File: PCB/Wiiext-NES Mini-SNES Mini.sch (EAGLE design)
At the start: 16 parts, among them J1 USB4085-GF-A_REVA4

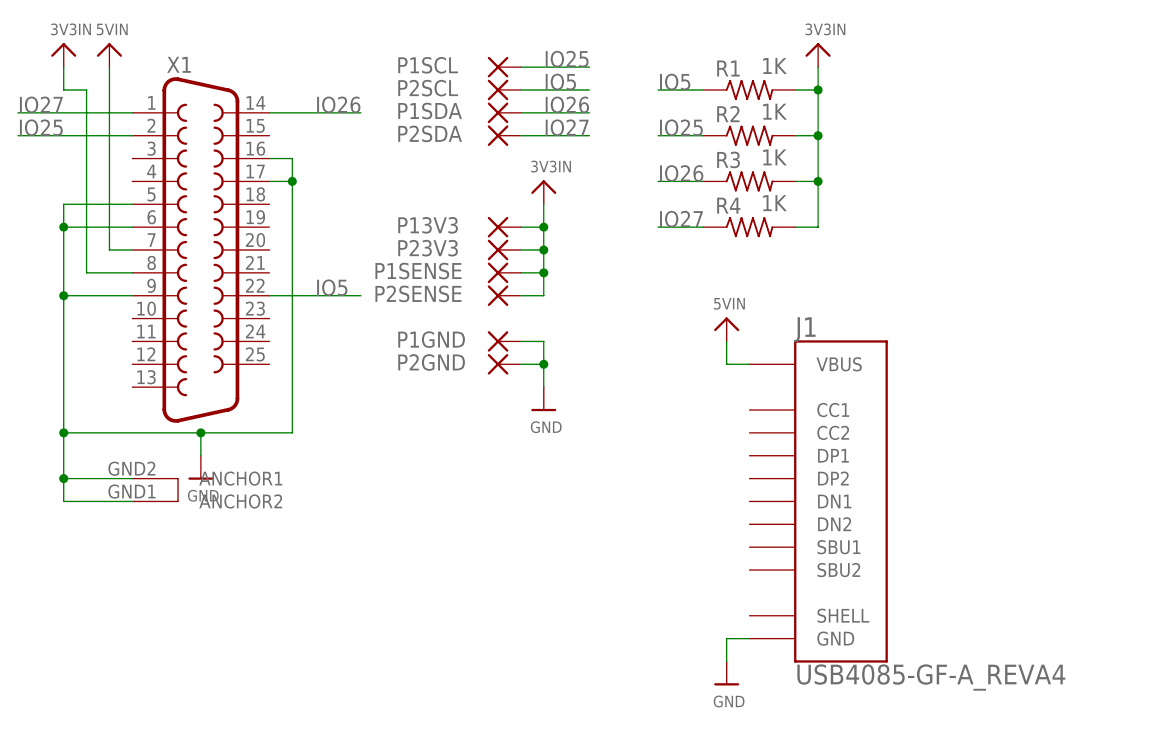
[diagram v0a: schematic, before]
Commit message: Add Support for 5V PD Chargers (#61)
Added 5.1K pull down resistors on the CC1 and CC2 to enable the use of a PD charger for 5V charging.  Also cleaned up the PCB design and spread out pads for easier assembly.
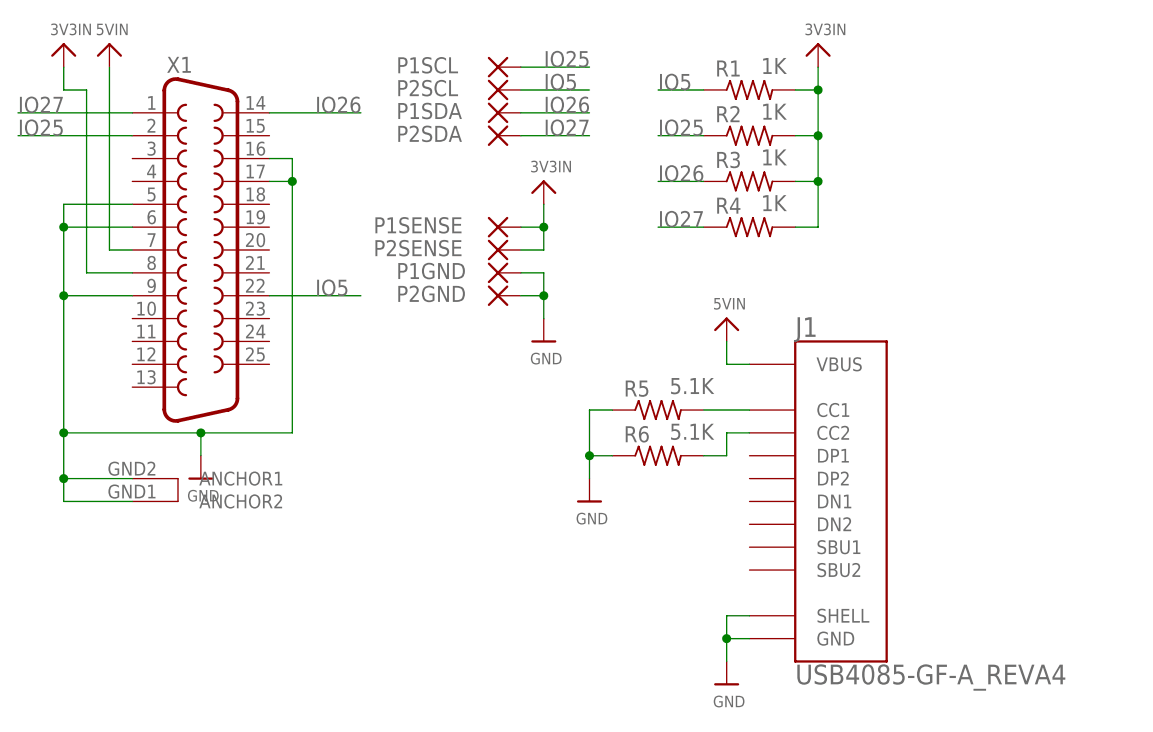
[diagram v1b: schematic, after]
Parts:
- removed P13V3, P23V3: (no value), wirepad:SMD5
- added R5, R6: 5.1K, adafruit:R-US_R1206
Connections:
- new net PD1: J1.CC2, R6.2
- new net PD2: J1.CC1, R5.2
- net 3V3IN: no longer P13V3.P, P23V3.P
- net GND: now also J1.SHELL, R5.1, R6.1
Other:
- moved on the sheet: P1GND, P1SENSE, P2GND, P2SENSE
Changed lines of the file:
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@@
 <part name="P1SDA" library="wirepad" library_urn="urn:adsk.eagle:library:412" deviceset="SMD5" device="" package3d_urn="urn:adsk.eagle:package:30841/1"/>
 <part name="P2SDA" library="wirepad" library_urn="urn:adsk.eagle:library:412" deviceset="SMD5" device="" package3d_urn="urn:adsk.eagle:package:30841/1"/>
-<part name="P13V3" library="wirepad" library_urn="urn:adsk.eagle:library:412" deviceset="SMD5" device="" package3d_urn="urn:adsk.eagle:package:30841/1"/>
-<part name="P23V3" library="wirepad" library_urn="urn:adsk.eagle:library:412" deviceset="SMD5" device="" package3d_urn="urn:adsk.eagle:package:30841/1"/>
 <part name="P1SENSE" library="wirepad" library_urn="urn:adsk.eagle:library:412" deviceset="SMD5" device="" package3d_urn="urn:adsk.eagle:package:30841/1"/>
 <part name="P1GND" library="wirepad" library_urn="urn:adsk.eagle:library:412" deviceset="SMD5" device="" package3d_urn="urn:adsk.eagle:package:30841/1"/>
@@
 <part name="U$4" library="Airquality_Sensor" library_urn="urn:adsk.eagle:library:16015176" deviceset="GND" device=""/>
 <part name="U$5" library="microbuilder" deviceset="VIN" device="" value="3V3IN"/>
+<part name="R5" library="adafruit" deviceset="R-US_" device="R1206" value="5.1K"/>
+<part name="R6" library="adafruit" deviceset="R-US_" device="R1206" value="5.1K"/>
+<part name="U$6" library="Airquality_Sensor" library_urn="urn:adsk.eagle:library:16015176" deviceset="GND" device=""/>
 </parts>
 <sheets>
@@
 <attribute name="VALUE" x="445.897" y="-3.302" size="1.778" layer="96"/>
 </instance>
-<instance part="P13V3" gate="1" x="447.04" y="-10.16" smashed="yes">
-<attribute name="NAME" x="435.737" y="-10.8458" size="1.778" layer="95"/>
+<instance part="P1SENSE" gate="1" x="447.04" y="-10.16" smashed="yes">
+<attribute name="NAME" x="433.197" y="-10.8458" size="1.778" layer="95"/>
 <attribute name="VALUE" x="445.897" y="-13.462" size="1.778" layer="96"/>
 </instance>
-<instance part="P23V3" gate="1" x="447.04" y="-12.7" smashed="yes">
-<attribute name="NAME" x="435.737" y="-13.3858" size="1.778" layer="95"/>
-<attribute name="VALUE" x="445.897" y="-16.002" size="1.778" layer="96"/>
-</instance>
-<instance part="P1SENSE" gate="1" x="447.04" y="-15.24" smashed="yes">
-<attribute name="NAME" x="433.197" y="-15.9258" size="1.778" layer="95"/>
+<instance part="P1GND" gate="1" x="447.04" y="-15.24" smashed="yes">
+<attribute name="NAME" x="435.737" y="-15.9258" size="1.778" layer="95"/>
 <attribute name="VALUE" x="445.897" y="-18.542" size="1.778" layer="96"/>
 </instance>
-<instance part="P1GND" gate="1" x="447.04" y="-22.86" smashed="yes">
-<attribute name="NAME" x="435.737" y="-23.5458" size="1.778" layer="95"/>
-<attribute name="VALUE" x="445.897" y="-26.162" size="1.778" layer="96"/>
-</instance>
-<instance part="P2GND" gate="1" x="447.04" y="-25.4" smashed="yes">
-<attribute name="NAME" x="435.737" y="-26.0858" size="1.778" layer="95"/>
-<attribute name="VALUE" x="445.897" y="-28.702" size="1.778" layer="96"/>
+<instance part="P2GND" gate="1" x="447.04" y="-17.78" smashed="yes">
+<attribute name="NAME" x="435.737" y="-18.4658" size="1.778" layer="95"/>
+<attribute name="VALUE" x="445.897" y="-21.082" size="1.778" layer="96"/>
 </instance>
 <instance part="P1SCL" gate="1" x="447.04" y="7.62" smashed="yes">
@@
 <attribute name="VALUE" x="445.897" y="1.778" size="1.778" layer="96"/>
 </instance>
-<instance part="U$52" gate="G$1" x="452.12" y="-30.48" smashed="yes">
-<attribute name="VALUE" x="450.596" y="-33.02" size="1.27" layer="96"/>
+<instance part="U$52" gate="G$1" x="452.12" y="-22.86" smashed="yes">
+<attribute name="VALUE" x="450.596" y="-25.4" size="1.27" layer="96"/>
 </instance>
 <instance part="U$55" gate="G$1" x="452.12" y="-5.08" smashed="yes">
@@
 <attribute name="VALUE" x="476.25" y="-8.382" size="1.778" layer="96"/>
 </instance>
-<instance part="P2SENSE" gate="1" x="447.04" y="-17.78" smashed="yes">
-<attribute name="NAME" x="433.197" y="-18.4658" size="1.778" layer="95"/>
-<attribute name="VALUE" x="445.897" y="-21.082" size="1.778" layer="96"/>
+<instance part="P2SENSE" gate="1" x="447.04" y="-12.7" smashed="yes">
+<attribute name="NAME" x="433.197" y="-13.3858" size="1.778" layer="95"/>
+<attribute name="VALUE" x="445.897" y="-16.002" size="1.778" layer="96"/>
 </instance>
 <instance part="U$1" gate="G$1" x="482.6" y="10.16" smashed="yes">
@@
 <instance part="U$5" gate="G$1" x="398.78" y="10.16" smashed="yes">
 <attribute name="VALUE" x="397.256" y="11.176" size="1.27" layer="96"/>
+</instance>
+<instance part="R5" gate="G$1" x="464.82" y="-30.48" smashed="yes">
+<attribute name="NAME" x="461.01" y="-28.9814" size="1.778" layer="95"/>
+<attribute name="VALUE" x="466.09" y="-28.702" size="1.778" layer="96"/>
+</instance>
+<instance part="R6" gate="G$1" x="464.82" y="-35.56" smashed="yes">
+<attribute name="NAME" x="461.01" y="-34.0614" size="1.778" layer="95"/>
+<attribute name="VALUE" x="466.09" y="-33.782" size="1.778" layer="96"/>
+</instance>
+<instance part="U$6" gate="G$1" x="457.2" y="-40.64" smashed="yes">
+<attribute name="VALUE" x="455.676" y="-43.18" size="1.27" layer="96"/>
 </instance>
 </instances>
@@
 <segment>
 <pinref part="P2GND" gate="1" pin="P"/>
-<wire x1="449.58" y1="-25.4" x2="452.12" y2="-25.4" width="0.1524" layer="91"/>
+<wire x1="449.58" y1="-17.78" x2="452.12" y2="-17.78" width="0.1524" layer="91"/>
 <pinref part="P1GND" gate="1" pin="P"/>
-<wire x1="449.58" y1="-22.86" x2="452.12" y2="-22.86" width="0.1524" layer="91"/>
+<wire x1="449.58" y1="-15.24" x2="452.12" y2="-15.24" width="0.1524" layer="91"/>
 <pinref part="U$52" gate="G$1" pin="GND"/>
-<wire x1="452.12" y1="-22.86" x2="452.12" y2="-25.4" width="0.1524" layer="91"/>
-<junction x="452.12" y="-25.4"/>
-<wire x1="452.12" y1="-25.4" x2="452.12" y2="-27.94" width="0.1524" layer="91"/>
+<wire x1="452.12" y1="-15.24" x2="452.12" y2="-17.78" width="0.1524" layer="91"/>
+<junction x="452.12" y="-17.78"/>
+<wire x1="452.12" y1="-17.78" x2="452.12" y2="-20.32" width="0.1524" layer="91"/>
 </segment>
 <segment>
@@
 <wire x1="472.44" y1="-55.88" x2="472.44" y2="-58.42" width="0.1524" layer="91"/>
 <pinref part="U$4" gate="G$1" pin="GND"/>
+<pinref part="J1" gate="G$1" pin="SHELL"/>
+<wire x1="474.98" y1="-53.34" x2="472.44" y2="-53.34" width="0.1524" layer="91"/>
+<wire x1="472.44" y1="-53.34" x2="472.44" y2="-55.88" width="0.1524" layer="91"/>
+<junction x="472.44" y="-55.88"/>
+</segment>
+<segment>
+<pinref part="R5" gate="G$1" pin="1"/>
+<wire x1="459.74" y1="-30.48" x2="457.2" y2="-30.48" width="0.1524" layer="91"/>
+<pinref part="U$6" gate="G$1" pin="GND"/>
+<wire x1="457.2" y1="-30.48" x2="457.2" y2="-35.56" width="0.1524" layer="91"/>
+<pinref part="R6" gate="G$1" pin="1"/>
+<wire x1="457.2" y1="-35.56" x2="457.2" y2="-38.1" width="0.1524" layer="91"/>
+<wire x1="459.74" y1="-35.56" x2="457.2" y2="-35.56" width="0.1524" layer="91"/>
+<junction x="457.2" y="-35.56"/>
 </segment>
 </net>
@@
 <segment>
 <pinref part="P1SENSE" gate="1" pin="P"/>
-<wire x1="449.58" y1="-15.24" x2="452.12" y2="-15.24" width="0.1524" layer="91"/>
-<pinref part="P23V3" gate="1" pin="P"/>
-<wire x1="449.58" y1="-12.7" x2="452.12" y2="-12.7" width="0.1524" layer="91"/>
-<pinref part="P13V3" gate="1" pin="P"/>
 <wire x1="449.58" y1="-10.16" x2="452.12" y2="-10.16" width="0.1524" layer="91"/>
 <pinref part="U$55" gate="G$1" pin="VIN"/>
-<wire x1="452.12" y1="-15.24" x2="452.12" y2="-12.7" width="0.1524" layer="91"/>
-<junction x="452.12" y="-12.7"/>
+<wire x1="452.12" y1="-10.16" x2="452.12" y2="-7.62" width="0.1524" layer="91"/>
+<pinref part="P2SENSE" gate="1" pin="P"/>
+<wire x1="449.58" y1="-12.7" x2="452.12" y2="-12.7" width="0.1524" layer="91"/>
 <wire x1="452.12" y1="-12.7" x2="452.12" y2="-10.16" width="0.1524" layer="91"/>
 <junction x="452.12" y="-10.16"/>
-<wire x1="452.12" y1="-10.16" x2="452.12" y2="-7.62" width="0.1524" layer="91"/>
-<pinref part="P2SENSE" gate="1" pin="P"/>
-<wire x1="449.58" y1="-17.78" x2="452.12" y2="-17.78" width="0.1524" layer="91"/>
-<wire x1="452.12" y1="-17.78" x2="452.12" y2="-15.24" width="0.1524" layer="91"/>
-<junction x="452.12" y="-15.24"/>
 </segment>
 <segment>
@@
 </segment>
 </net>
+<net name="PD2" class="0">
+<segment>
+<pinref part="R5" gate="G$1" pin="2"/>
+<pinref part="J1" gate="G$1" pin="CC1"/>
+<wire x1="469.9" y1="-30.48" x2="474.98" y2="-30.48" width="0.1524" layer="91"/>
+</segment>
+</net>
+<net name="PD1" class="0">
+<segment>
+<pinref part="J1" gate="G$1" pin="CC2"/>
+<wire x1="474.98" y1="-33.02" x2="472.44" y2="-33.02" width="0.1524" layer="91"/>
+<wire x1="472.44" y1="-33.02" x2="472.44" y2="-35.56" width="0.1524" layer="91"/>
+<pinref part="R6" gate="G$1" pin="2"/>
+<wire x1="472.44" y1="-35.56" x2="469.9" y2="-35.56" width="0.1524" layer="91"/>
+</segment>
+</net>
